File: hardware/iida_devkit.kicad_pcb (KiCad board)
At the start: 6 copper layers, 178.2 x 76.8 mm, 267 parts, among them J1001 132134, J201 USB4105-GF-A, J202 PRPC001DAAN-RC, J301 B2B-XH-A, J302 PRPC001DAAN-RC, J401 61300111121, J402 PRPC001DAAN-RC, J403 PRPC001DAAN-RC, J404 PRPC001DAAN-RC, J501 PRPC006SAAN-RC, J502 TC2050, J503 61300611121, J504 61300611121, J505 61300611121, J506 61300611121, J507 61300611121, J508 PRPC001DAAN-RC, J509 PRPC006SAAN-RC, J901 SIM8066-6-1-14-01-A, Q301 IRLML6401TRPBF, Q302 DMN2005, Q303 DMN2005, Q501 BSS806NH, Q801 BSS806NH, Q802 IRLML6401TRPBF, Q803 BSS806NH, Q804 BSS806NH, Q805 BSS806NH, U201 USBLC6-2SC6, U301 BQ29728DSER, U302 MCP73833T-FCI/MF, U303 MAX17048G+T10, U401 LM66200DRLR, U402 TPS63020DSJR, U403 LD39200DPUR, U501 STM32L552CEU6, U502 AT25SF081B-MAHB-T, U601 MCP9808T-E/MC, U602 SHT40-AD1B-R2, U701 TCA9554PW, U801 SN74AVC4T774, U802 SARA-R500S-01B, Y501 ECS-160-9-37-CKM-TR3, Y502 ABS05-32.768KHZ-9-T

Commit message: HW: Layout power, gpios and such
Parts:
- removed TP307, TP308, TP309, TP310, TP311, TP312, TP601: TestPoint, TestPoint:TestPoint_Pad_D1.0mm
- removed U201: USBLC6-2SC6, Package_TO_SOT_SMD:SOT-23-6
- added D201: DF2B5M4CT,L3F, Diode_SMD:D_SOD-882D, F.Cu at (99.4, 112.8)
- added D202: DF2B5M4CT,L3F, Diode_SMD:D_SOD-882D, F.Cu at (97.5, 112.8)
- added D203: SMAJ6.0CA, Diode_SMD:D_SMA, F.Cu at (90.3, 118.9)
- moved C409 126.3 mm to (101.0, 79.8), turned to -90 degrees
- moved R405 124.2 mm to (99.7, 79.7), turned to -90 degrees
- moved C410 121.7 mm to (108.6, 75.8), turned to 90 degrees
- moved C411 121.6 mm to (108.3, 78.3), turned to -90 degrees
- moved R406 117.8 mm to (107.6, 75.8), turned to 90 degrees
- moved R407 113.8 mm to (107.6, 73.9), turned to 90 degrees
- moved U403 112.4 mm to (104.4, 75.9), turned to 180 degrees
- moved R509 80.0 mm to (158.2, 107.0)
- moved R508 80.0 mm to (158.2, 106.0)
- moved R401 72.8 mm to (90.2, 80.1), turned to 0 degrees
- moved C602 72.2 mm to (113.1, 94.5), turned to 0 degrees
- moved C402 72.2 mm to (86.6, 74.1), turned to 90 degrees
- moved C406 72.0 mm to (97.0, 75.9)
- moved C407 72.0 mm to (98.5, 75.9)
- moved C408 72.0 mm to (100.0, 75.9)
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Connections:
- J201 pad A6: /USB/USB_DP_IN -> /Microcontroller/USB_DP
- J201 pad A7: /USB/USB_DN_IN -> /Microcontroller/USB_DN
- J201 pad B6: /USB/USB_DP_IN -> /Microcontroller/USB_DP
- J201 pad B7: /USB/USB_DN_IN -> /Microcontroller/USB_DN
- J503 pad 1: /Microcontroller/GPIO_PB12 -> /Microcontroller/GPIO_PA9
- J503 pad 3: /Microcontroller/GPIO_PB15 -> /Microcontroller/GPIO_PA8
- J503 pad 5: /Microcontroller/GPIO_PA8 -> /Microcontroller/GPIO_PB15
- J504 pad 1: /Microcontroller/GPIO_PA9 -> /Microcontroller/GPIO_PA10
- J504 pad 3: /Microcontroller/GPIO_PA10 -> /Microcontroller/GPIO_PA15
- J504 pad 5: /Microcontroller/GPIO_PA15 -> /Microcontroller/GPIO_PB4
- J505 pad 1: /Microcontroller/GPIO_PB4 -> /Microcontroller/GPIO_PB5
- J505 pad 3: /Microcontroller/GPIO_PB5 -> /Microcontroller/GPIO_PB8
- J505 pad 5: /Microcontroller/GPIO_PB8 -> /Microcontroller/GPIO_PB9
- J506 pad 1: /Microcontroller/GPIO_PB9 -> /Microcontroller/GPIO_PB12
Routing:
- net /Battery/I2C_SDA: track 0.00 -> 83.2 mm, vias 0 -> 5
- net GND: track 0.00 -> 69.5 mm, vias 0 -> 308
- net /Battery/I2C_SCL: track 0.00 -> 68.5 mm, vias 0 -> 4
- net /Microcontroller/GPIO_PA9: track 0.00 -> 65.9 mm, vias 0 -> 2
- net /Microcontroller/GPIO_PA8: track 0.00 -> 59.7 mm, vias 0 -> 2
- net /Battery/BATT+: track 0.00 -> 53.3 mm, vias 0 -> 1
- net /Microcontroller/GPIO_PB15: track 0.00 -> 49.7 mm, vias 0 -> 1
- net /Microcontroller/USB_DP: track 0.00 -> 46.3 mm
- net /Microcontroller/USB_DN: track 0.00 -> 45.9 mm
- net /IO expander/IO_EXP_INT: track 0.00 -> 45.4 mm, vias 0 -> 4
- net /Microcontroller/GPIO_PB12: track 0.00 -> 37.8 mm, vias 0 -> 2
- net /Microcontroller/GPIO_PB2: track 0.00 -> 37.1 mm, vias 0 -> 2
- net /Microcontroller/BOOT0: track 0.00 -> 30.2 mm, vias 0 -> 2
- net /Microcontroller/NRST: track 0.00 -> 29.2 mm, vias 0 -> 2
- net Net-(D302-K): track 0.00 -> 28.7 mm, vias 0 -> 2
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- added copper zone on In2.Cu, net /Battery/BATT+
- added copper zone on In4.Cu, net /Battery/BATT+
- added copper zone on In2.Cu, net /Battery/BATT-
- added copper zone on In4.Cu, net /Battery/BATT-
- added copper zone on In2.Cu, net /Battery/V_5V0
- added copper zone on In4.Cu, net /Battery/V_5V0
- added copper zone on In2.Cu, net /Battery/V_BAT
- added copper zone on In4.Cu, net /Battery/V_BAT
- added copper zone on F.Cu, net /Power/V_3V7
- added copper zone on In2.Cu, net /Power/V_3V7
- added copper zone on In4.Cu, net /Power/V_3V7
- added copper zone on F.Cu, net /Power/V_SYS
- added copper zone on In2.Cu, net /Power/V_SYS
- added copper zone on In4.Cu, net /Power/V_SYS
- added copper zone on In2.Cu, net /USB/VBUS
- added copper zone on In4.Cu, net /USB/VBUS
- added copper zone on In2.Cu, net Net-(Q301-D)
- added copper zone on In4.Cu, net Net-(Q301-D)
- added copper zone on In2.Cu, net Net-(Q302-D)
- added copper zone on In4.Cu, net Net-(Q302-D)
- added copper zone on In2.Cu, net V_3V3
- added copper zone on In4.Cu, net V_3V3
- removed copper zone on F.Cu, net /Battery/BAT_PROT_IN
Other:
- board text added: "PA10→"
- board text added: "PB8→"
- board text added: "PB9→"
- board text added: "←PA8"
- board text added: "←PA9"
- board text removed: "PA8→"
- board text removed: "PB6→"
- board text removed: "PB7→"
- board text removed: "←PB13"
- board text removed: "←PB14"

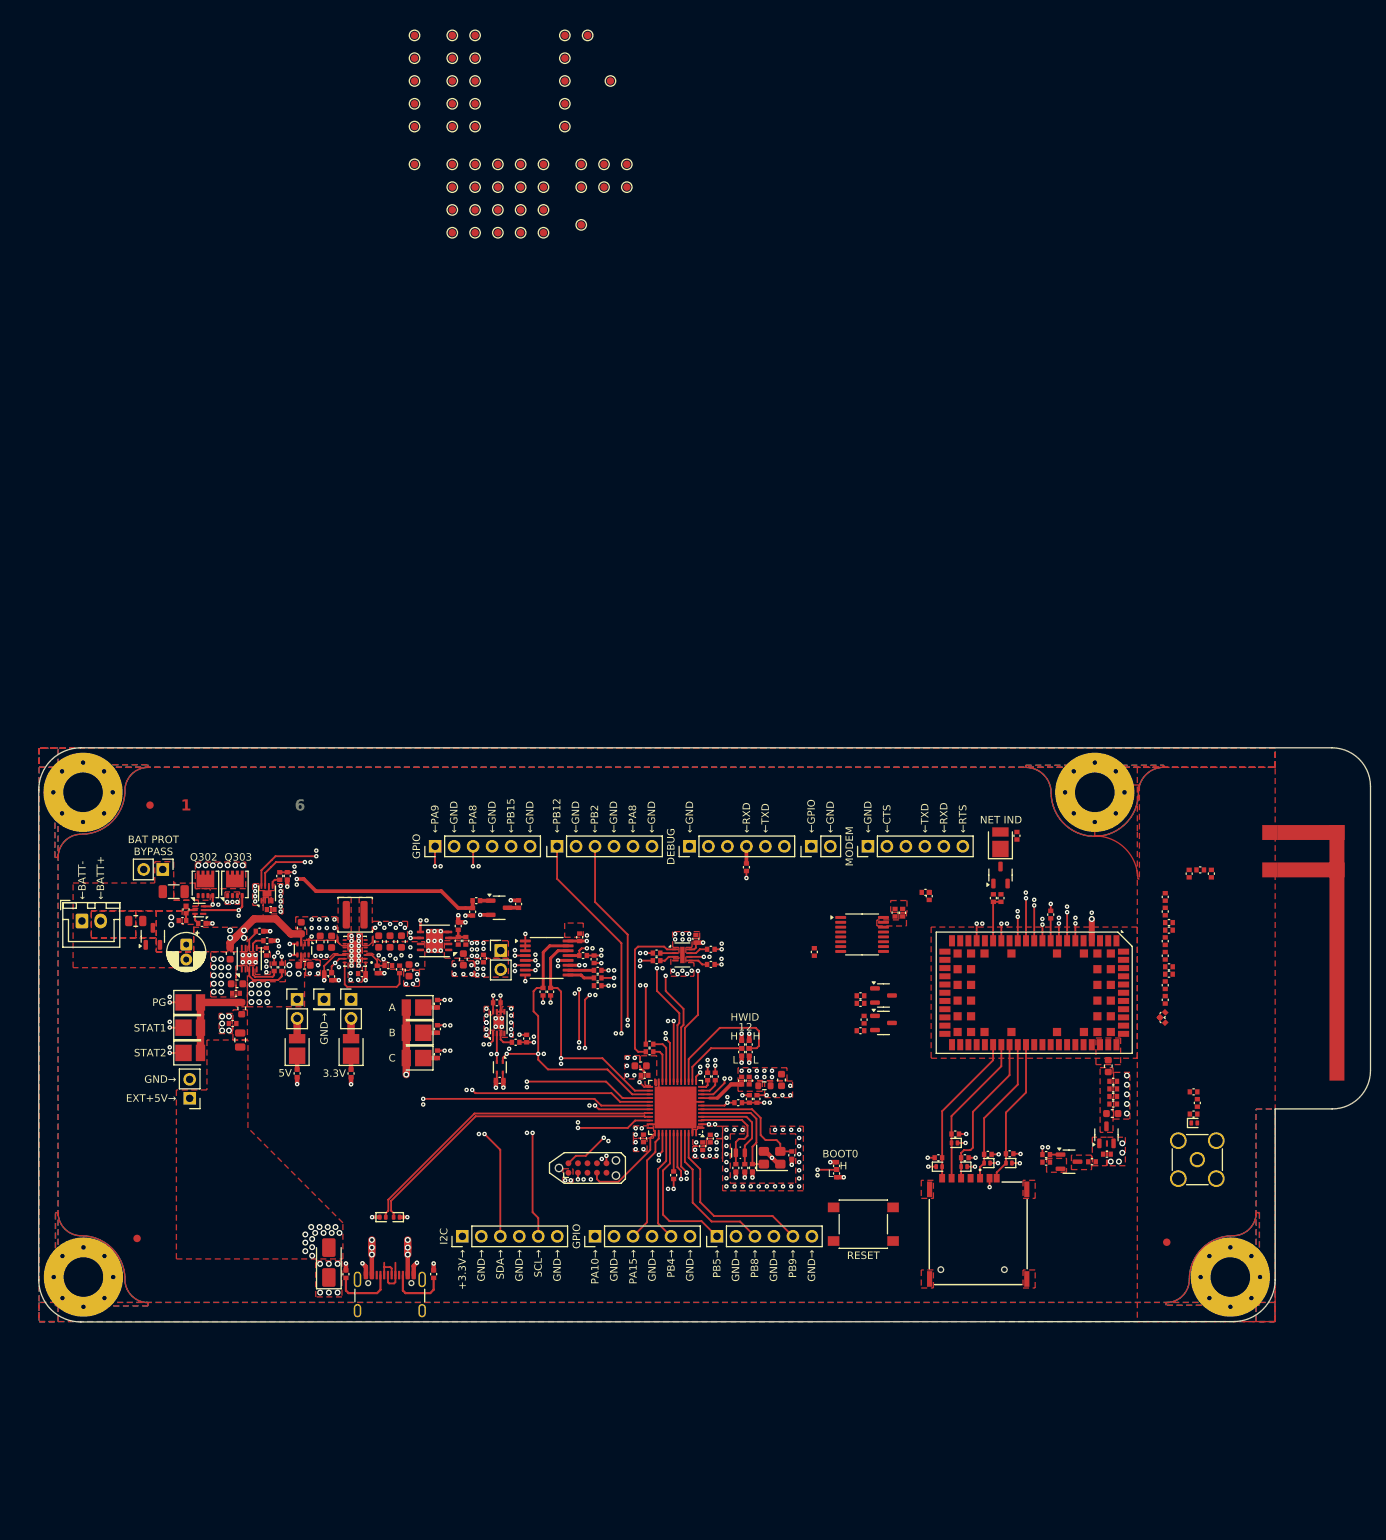
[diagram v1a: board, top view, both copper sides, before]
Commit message: HW: Route interconnects
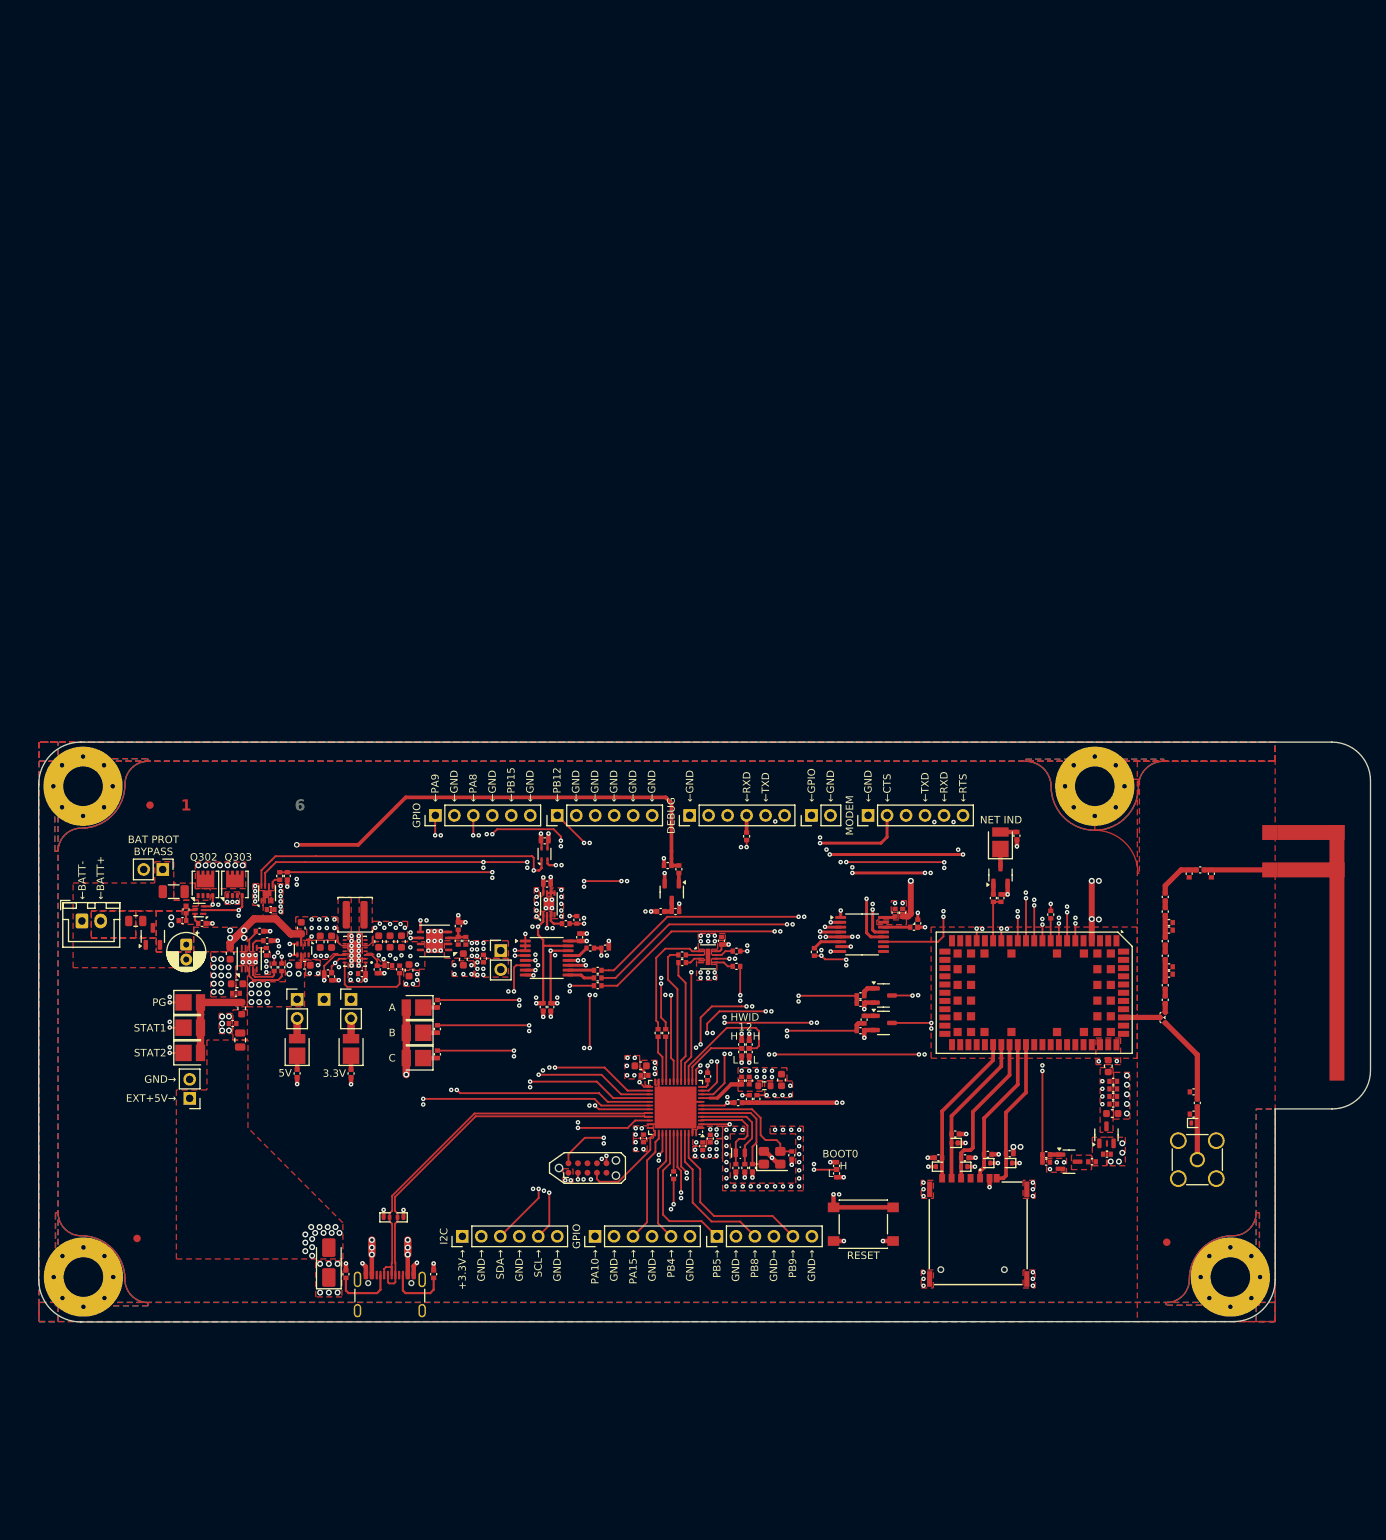
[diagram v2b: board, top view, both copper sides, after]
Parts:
- removed TP201, TP301, TP302, TP303, TP304, TP305, TP306, TP313, TP401, TP402, TP403, TP404, TP405, TP406, TP407, TP408, TP409, TP410, TP501, TP502, TP503, TP504, TP505, TP506, TP701, TP801, TP802, TP803, TP804, TP805, TP806, TP807, TP808, TP809, TP810, TP811, TP812, TP813, TP814, TP815, TP816, TP817, TP818, TP819, TP820, TP901, TP902, TP903, TP904, TP905: TestPoint, TestPoint:TestPoint_Pad_D1.0mm
- J401: moved to B.Cu
- moved C602 32.6 mm to (119.2, 62.5), turned to 180 degrees
- moved U602 29.2 mm to (119.1, 64.2), turned to 90 degrees
- moved NT301 28.9 mm to (136.1, 64.4), turned to -90 degrees
- moved R503 27.4 mm to (137.1, 66.3), turned to -90 degrees
- moved R502 26.8 mm to (135.6, 65.8), turned to 180 degrees
- moved R506 23.2 mm to (134.7, 71.9), turned to 180 degrees
- moved Q501 23.2 mm to (136.2, 69.3), turned to -90 degrees
- moved R505 21.0 mm to (136.7, 71.9), turned to 180 degrees
- moved R602 17.2 mm to (122.0, 73.5)
- moved C601 17.2 mm to (119.5, 68.3)
- moved R601 17.2 mm to (123.5, 73.0)
- moved U601 17.2 mm to (119.7, 70.9)
- moved R810 4.91 mm to (168.6, 74.0)
- moved J501 4.14 mm to (138.6, 59.1)
- moved J503 4.14 mm to (104.5, 59.1)
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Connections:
- J506 pad 3: /Microcontroller/GPIO_PB2 -> GND
- U501 pad 20: /Microcontroller/GPIO_PB2 -> unconnected-(U501A-PB2-Pad20)
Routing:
- net /IO expander/MDM_PWR_EN: track 1.93 -> 92.8 mm, vias 2 -> 4
- net /Microcontroller/MDM_RXD: track 6.34 -> 96.8 mm, vias 1 -> 5
- net /Microcontroller/MDM_TXD: track 1.33 -> 88.8 mm, vias 1 -> 5
- net /Modem/V_1V8_MDM: track 3.87 -> 78.6 mm, vias 2 -> 4
- net /Battery/BAT_MON_INTn: track 3.33 -> 63.2 mm, vias 2 -> 4
- net /IO expander/MDM_RESET: track 1.68 -> 53.2 mm, vias 1 -> 2
- net /IO expander/MDM_PWR_ON: track 0.95 -> 48.7 mm, vias 1 -> 2
- net /Microcontroller/DBG_GPIO: track 4.35 -> 51.2 mm, vias 1 -> 3
- net /Battery/I2C_SCL: track 68.5 -> 113.6 mm, vias 4 -> 8
- net /Battery/BATT+: track 53.3 -> 94.1 mm, vias 1 -> 2
- net /Microcontroller/DBG_UART_TX: track 0.95 -> 41.3 mm, vias 1 -> 3
- net /Microcontroller/GPIO_PB2: track 37.1 -> 0.00 mm, vias 2 -> 0
- net /Microcontroller/DBG_UART_RX: track 2.41 -> 38.6 mm, vias 2 -> 4
- net /Microcontroller/MDM_RTS: track 0.00 -> 35.1 mm, vias 0 -> 3
- net /Battery/I2C_SDA: track 83.2 -> 117.6 mm
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- added copper zone on In2.Cu, net /Modem/VCC
- added copper zone on In2.Cu, net /Modem/VCC_FILTERING
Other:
- board size 178.2 x 76.8 mm -> 178.2 x 77.6 mm
- board text removed: "←PB2"

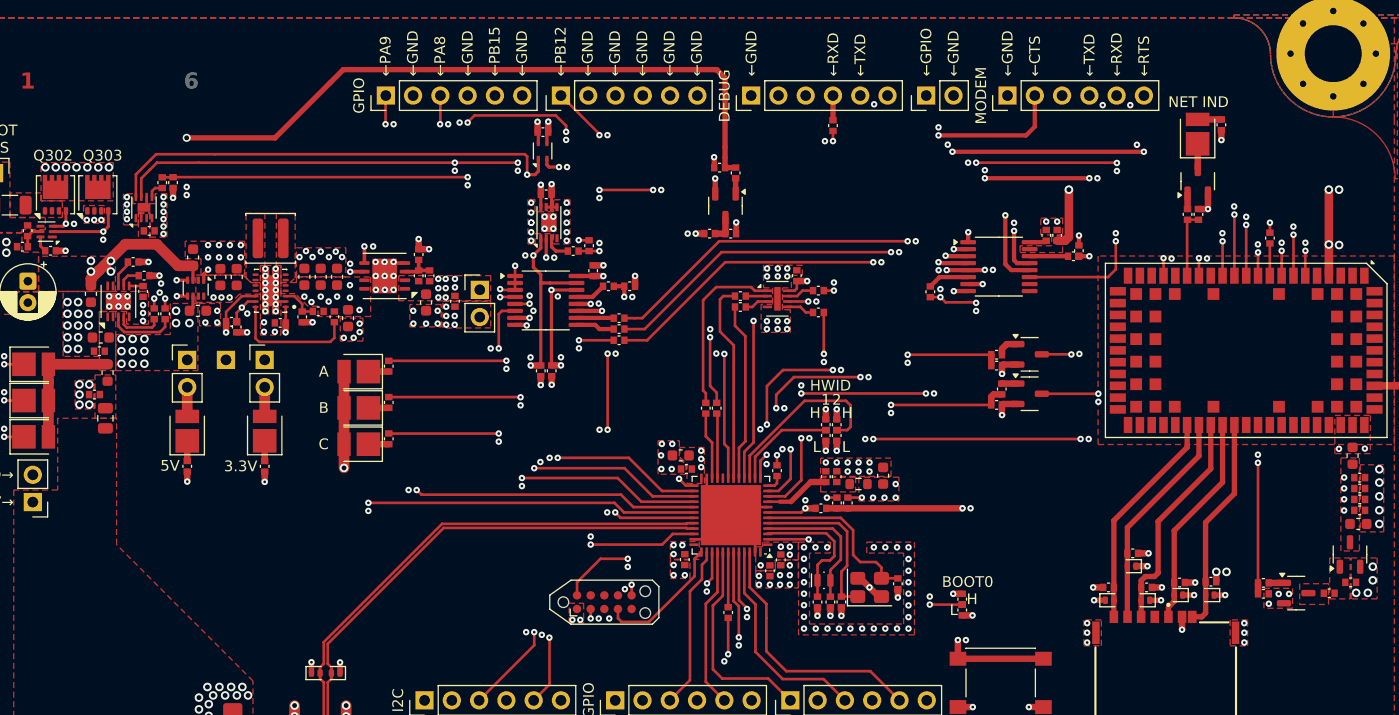
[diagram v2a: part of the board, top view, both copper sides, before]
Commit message: HW: Convert to 4 layers
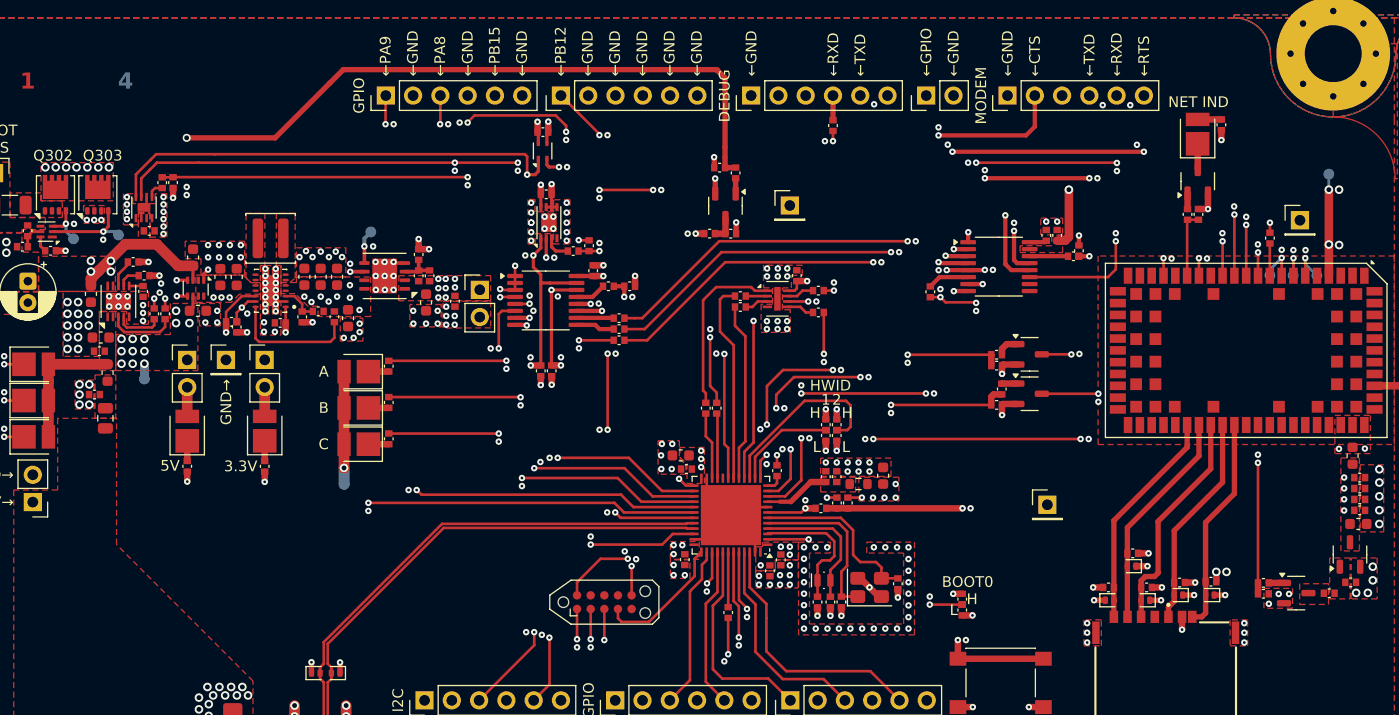
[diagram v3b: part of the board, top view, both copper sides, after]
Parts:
- added J401: 61300111121, Connector_PinHeader_2.54mm:PinHeader_1x01_P2.54mm_Vertical, F.Cu at (166.1, 97.2)
- added J404: 61300111121, Connector_PinHeader_2.54mm:PinHeader_1x01_P2.54mm_Vertical, F.Cu at (142.2, 69.3)
- added J407: 61300111121, Connector_PinHeader_2.54mm:PinHeader_1x01_P2.54mm_Vertical, F.Cu at (189.7, 70.7)
- added TP301: TestPoint, TestPoint:TestPoint_Pad_D1.0mm, B.Cu at (75.5, 72.4)
- added TP302: TestPoint, TestPoint:TestPoint_Pad_D1.0mm, B.Cu at (79.6, 72.0)
- added TP402: TestPoint, TestPoint:TestPoint_Pad_D1.0mm, B.Cu at (103.1, 71.8)
- added TP403: TestPoint, TestPoint:TestPoint_Pad_D1.0mm, B.Cu at (100.6, 95.3)
- added TP404: TestPoint, TestPoint:TestPoint_Pad_D1.0mm, B.Cu at (82.1, 85.5)
- added TP801: TestPoint, TestPoint:TestPoint_Pad_D1.0mm, B.Cu at (191.2, 75.8)
- added TP802: TestPoint, TestPoint:TestPoint_Pad_D1.0mm, B.Cu at (189.0, 75.8)
- added TP803: TestPoint, TestPoint:TestPoint_Pad_D1.0mm, B.Cu at (186.9, 75.8)
- added TP804: TestPoint, TestPoint:TestPoint_Pad_D1.0mm, B.Cu at (192.3, 66.4)
- J402: renamed from J401; moved to F.Cu
- renumbered J402 to J403, J403 to J405, J404 to J406, R505 to R504, R504 to R505, R806 to R805, R805 to R806
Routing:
- net V_3V3: track 32.6 -> 36.9 mm, vias 43 -> 42
- net /Microcontroller/DEBUG_SWDIO: track 17.8 -> 21.7 mm
- net GND: track 85.3 -> 88.2 mm, vias 367 -> 368
- net /Microcontroller/DEBUG_SWO: track 11.6 -> 13.5 mm
- net /Battery/D_{OUT}: track 2.51 -> 4.21 mm
- net Net-(U403-PG): track 1.55 -> 3.14 mm
- net /Battery/C_{OUT}: track 6.82 -> 8.37 mm
- net /Modem/V_1V8_MDM: track 78.6 -> 80.1 mm
- net /Battery/V_5V0: track 13.8 -> 15.2 mm
- net /Modem/DCD: track 2.32 -> 3.74 mm
- net /Modem/DSR: track 2.33 -> 3.71 mm
- net /Modem/RI: track 3.82 -> 3.25 mm
- removed copper zone on In4.Cu, net /Battery/BATT+
- removed copper zone on In4.Cu, net /Battery/BATT-
- removed copper zone on In4.Cu, net /Battery/V_5V0
- removed copper zone on In4.Cu, net /Battery/V_BAT
- removed copper zone on In4.Cu, net /Microcontroller/VDDA
- removed copper zone on In4.Cu, net /Power/V_3V7
- removed copper zone on In4.Cu, net /Power/V_SYS
- removed copper zone on In4.Cu, net /USB/VBUS
- removed copper zone on In3.Cu, net GND
- removed copper zone on In4.Cu, net GND
- removed copper zone on In4.Cu, net Net-(Q301-D)
- removed copper zone on In4.Cu, net Net-(Q302-D)
- removed copper zone on In4.Cu, net V_3V3
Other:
- copper layers 6 -> 4
- board text added: "C_{OUT}"
- board text added: "DCD→"
- board text added: "DSR→"
- board text added: "D_{OUT}"
- board text added: "RI→"
- board text added: "V_3V3→"
- board text added: "V_5V0→"
- board text added: "←PG"
- board text added: "←V_1V8_MDM"
- board text removed: "5"
- board text removed: "6"
